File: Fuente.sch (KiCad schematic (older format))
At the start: 18 parts, among them J5 TB_1X2, P2 USB_OTG, U2 LM2596-5.0, U3 NCP1117ST33T3G

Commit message: Modifico algunos componentes. Seteo algunos encapsulados. Ordeno los componentes en el PCB.
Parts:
- removed TH1: PTS18126V300, ~, symbol THERMISTOR-RESCUE-ciaa-nxp
- removed U2: LM2596-5.0, ~, symbol LM2596-5.0
- removed ZA1: P6SMB33CA, ~, symbol TVS-RESCUE-ciaa-nxp
- added U2: LM2576HVS-5, TO_SOT_Packages_SMD:TO-263-5Lead, symbol LM2576HVS-5
- C6: footprint ~ -> Capacitors_ThroughHole:C_Radial_D13_L21_P5
- C7: value 330uF -> 1000uF; footprint ~ -> Capacitors_ThroughHole:C_Radial_D10_L20_P5
- C8: footprint ~ -> Capacitors_ThroughHole:C_Radial_D10_L25_P5
- D1, D3, FB1, FB2: footprint ~ -> Diodes_SMD:SOD-123
- D2: value B540C-13-F -> 1N5822; footprint ~ -> Diodes_SMD:SOD-123
- D4: footprint ~ -> LEDs:LED_1206
- J5: footprint ~ -> Connect:bornier2
- L1: value 47uH -> 100uH; footprint ~ -> Inductors:INDUCTOR_V
- P2: footprint (none) -> Connect:USB_Micro-B
- R1: footprint ~ -> SMD_Packages:SMD-1206_Pol
- U3: footprint ~ -> TO_SOT_Packages_SMD:SOT-323
- ZA2: footprint ~ -> Diodes_SMD:SMB_Handsoldering
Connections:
- net labels removed: +24V
- wire segments 47 -> 45
- no-connect marks 4 -> 5
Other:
- note removed: "Polyswitch"
- moved on the sheet: C6, D1, J5

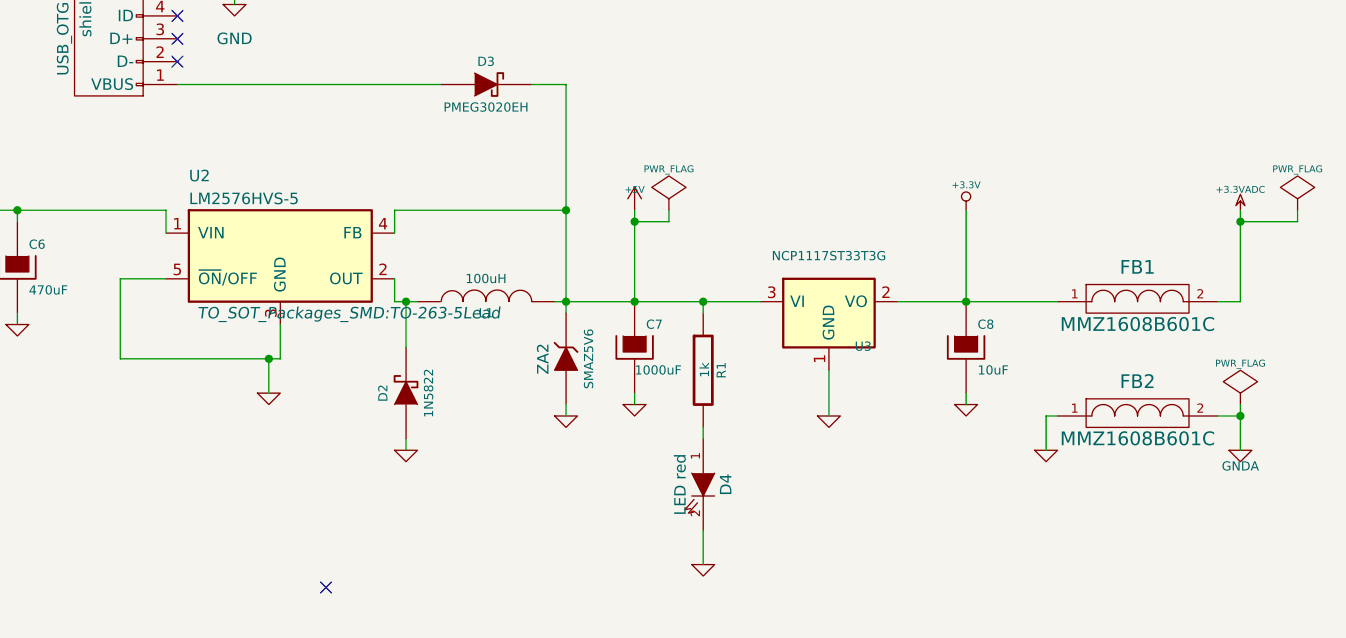
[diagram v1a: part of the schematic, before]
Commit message: Algunas modificaciones en el circuito  oreno el pcb.
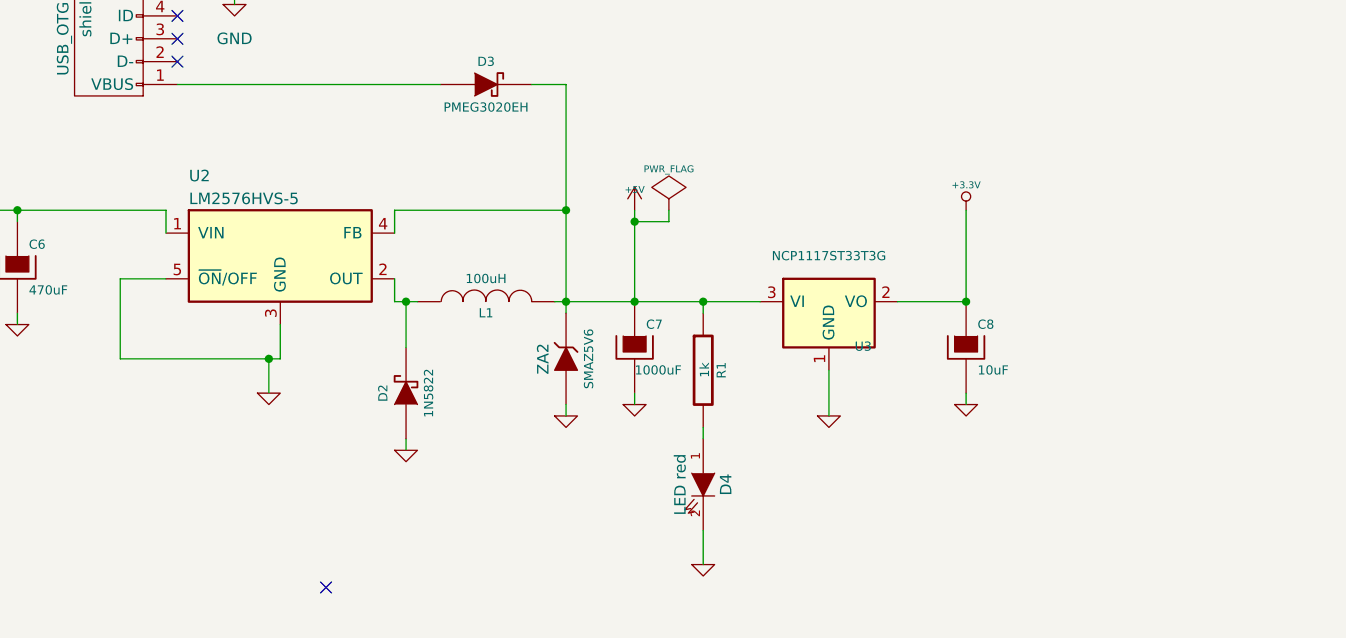
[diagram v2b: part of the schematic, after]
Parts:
- removed FB1, FB2: MMZ1608B601C, Diodes_SMD:SOD-123, symbol FILTER
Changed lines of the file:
@@
 LIBS:video
 LIBS:xilinx
+LIBS:sim800l
 EELAYER 25 0
 EELAYER END
@@
 encoding utf-8
 Sheet 3 6
-Title "CIAA Fuente de alimentación"
+Title "Fuente de alimentación"
 Date "11 may 2015"
 Rev "1.0"
@@
 Connection ~ 6900 3650
 Connection ~ 8050 3650
-Wire Wire Line
-	7750 3650 8450 3650
 $Comp
 L GND-RESCUE-ciaa-nxp #PWR014
@@
 	6300 4150 6300 4100
 $Comp
-L FILTER FB1
-U 1 1 581A28AB
-P 8800 3650
-F 0 "FB1" H 8800 3800 60  0000 C CNN
-F 1 "MMZ1608B601C" H 8800 3550 60  0000 C CNN
-F 2 "Diodes_SMD:SOD-123" H 8800 3650 60  0001 C CNN
-F 3 "~" H 8800 3650 60  0000 C CNN
-	1    8800 3650
-	1    0    0    -1
-$EndComp
-Wire Wire Line
-	9250 3650 9150 3650
-Wire Wire Line
-	9250 3250 9250 3650
-$Comp
 L +5V #PWR015
 U 1 1 581A28AD
@@
 $EndComp
 $Comp
-L +3.3VADC #PWR017
-U 1 1 581A28AF
-P 9250 3250
-F 0 "#PWR017" H 9250 3370 20  0001 C CNN
-F 1 "+3.3VADC" H 9250 3340 30  0000 C CNN
-F 2 "" H 9250 3250 60  0000 C CNN
-F 3 "" H 9250 3250 60  0000 C CNN
-	1    9250 3250
-	1    0    0    -1
-$EndComp
-$Comp
-L FILTER FB2
-U 1 1 581A28B0
-P 8800 4150
-F 0 "FB2" H 8800 4300 60  0000 C CNN
-F 1 "MMZ1608B601C" H 8800 4050 60  0000 C CNN
-F 2 "Diodes_SMD:SOD-123" H 8800 4150 60  0001 C CNN
-F 3 "~" H 8800 4150 60  0000 C CNN
-	1    8800 4150
-	1    0    0    -1
-$EndComp
-$Comp
-L GND-RESCUE-ciaa-nxp #PWR018
-U 1 1 581A28B1
-P 8400 4300
-F 0 "#PWR018" H 8400 4300 30  0001 C CNN
-F 1 "GND" H 8400 4230 30  0001 C CNN
-F 2 "" H 8400 4300 60  0000 C CNN
-F 3 "" H 8400 4300 60  0000 C CNN
-	1    8400 4300
-	1    0    0    -1
-$EndComp
-Wire Wire Line
-	8400 4150 8450 4150
-$Comp
-L GNDA-RESCUE-ciaa-nxp #PWR019
-U 1 1 581A28B2
-P 9250 4300
-F 0 "#PWR019" H 9250 4300 40  0001 C CNN
-F 1 "GNDA" H 9250 4230 40  0000 C CNN
-F 2 "" H 9250 4300 60  0000 C CNN
-F 3 "" H 9250 4300 60  0000 C CNN
-	1    9250 4300
-	1    0    0    -1
-$EndComp
-Wire Wire Line
-	9250 4100 9250 4300
-Wire Wire Line
-	9250 4150 9150 4150
-$Comp
-L PWR_FLAG #FLG020
+L PWR_FLAG #FLG017
 U 1 1 581A28B3
 P 6750 3250
-F 0 "#FLG020" H 6750 3345 30  0001 C CNN
+F 0 "#FLG017" H 6750 3345 30  0001 C CNN
 F 1 "PWR_FLAG" H 6750 3430 30  0000 C CNN
 F 2 "" H 6750 3250 60  0000 C CNN
@@
 	6750 3300 6600 3300
 Connection ~ 6600 3300
-$Comp
-L PWR_FLAG #FLG021
-U 1 1 581A28B4
-P 9500 3250
-F 0 "#FLG021" H 9500 3345 30  0001 C CNN
-F 1 "PWR_FLAG" H 9500 3430 30  0000 C CNN
-F 2 "" H 9500 3250 60  0000 C CNN
-F 3 "" H 9500 3250 60  0000 C CNN
-	1    9500 3250
-	1    0    0    -1
-$EndComp
-Wire Wire Line
-	9500 3250 9500 3300
-Wire Wire Line
-	9500 3300 9250 3300
-Connection ~ 9250 3300
-$Comp
-L PWR_FLAG #FLG022
-U 1 1 581A28B5
-P 9250 4100
-F 0 "#FLG022" H 9250 4195 30  0001 C CNN
-F 1 "PWR_FLAG" H 9250 4280 30  0000 C CNN
-F 2 "" H 9250 4100 60  0000 C CNN
-F 3 "" H 9250 4100 60  0000 C CNN
-	1    9250 4100
-	1    0    0    -1
-$EndComp
-Connection ~ 9250 4150
-Wire Wire Line
-	8400 4150 8400 4300
 Wire Wire Line
 	3500 3450 3500 3700
 $Comp
-L PWR_FLAG #FLG023
+L PWR_FLAG #FLG018
 U 1 1 581A28B7
 P 3350 3700
-F 0 "#FLG023" H 3350 3795 30  0001 C CNN
+F 0 "#FLG018" H 3350 3795 30  0001 C CNN
 F 1 "PWR_FLAG" H 3350 3880 30  0000 C CNN
 F 2 "" H 3350 3700 60  0000 C CNN
@@
 $EndComp
 $Comp
-L GND #PWR024
+L GND #PWR019
 U 1 1 581A28BC
 P 4850 2350
-F 0 "#PWR024" H 4850 2100 50  0001 C CNN
+F 0 "#PWR019" H 4850 2100 50  0001 C CNN
 F 1 "GND" H 4850 2200 50  0000 C CNN
 F 2 "" H 4850 2350 50  0000 C CNN
@@
 F 0 "U2" H 4650 3800 50  0000 L CNN
 F 1 "LM2576HVS-5" H 4650 3700 50  0000 L CNN
-F 2 "TO_SOT_Packages_SMD:TO-263-5Lead" H 5350 3200 50  0000 C CIN
+F 2 "TO_SOT_Packages_SMD:TO-263-5Lead" H 5350 3200 50  0001 C CIN
 F 3 "" H 5050 3450 50  0000 C CNN
 	1    5050 3450
@@
 Connection ~ 3900 3250
 NoConn ~ 5250 4900
+Wire Wire Line
+	7750 3650 8050 3650
 $EndSCHEMATC

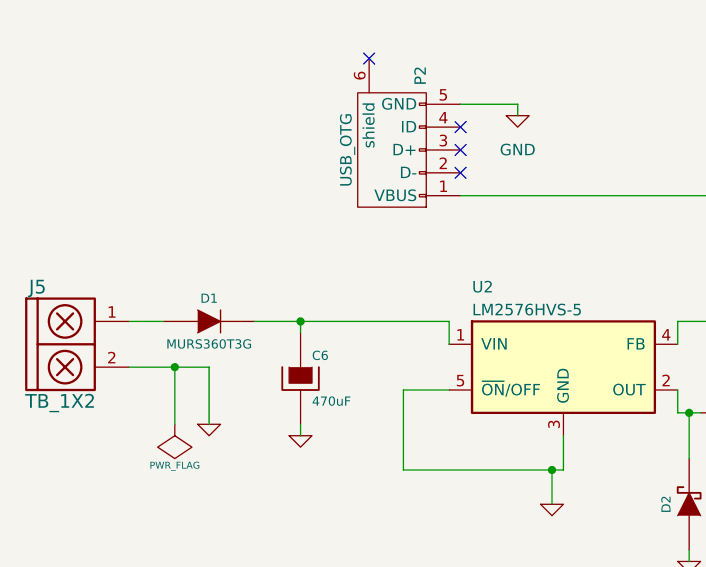
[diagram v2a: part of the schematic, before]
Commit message: Modificaciones en el schematic debida a los warning por powerflag y conectores mal definido como input en vez de pasive.
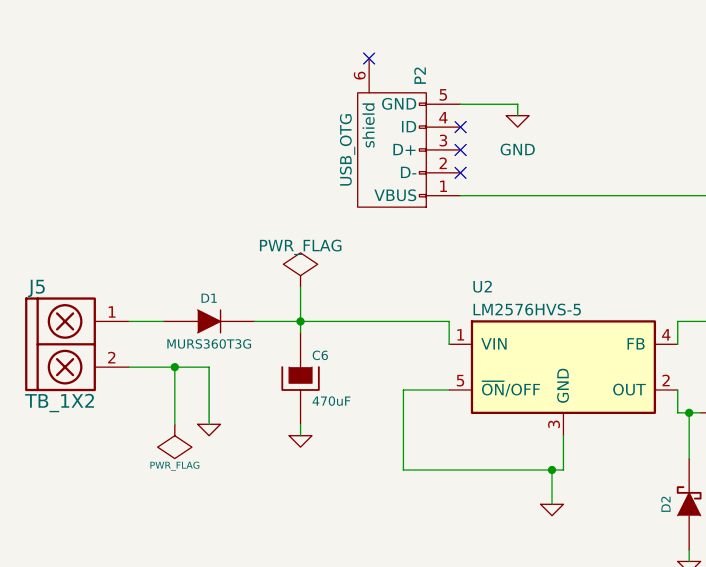
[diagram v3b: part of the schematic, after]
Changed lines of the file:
@@
 $Descr A4 11693 8268
 encoding utf-8
-Sheet 3 6
+Sheet 3 5
 Title "Fuente de alimentación"
 Date "11 may 2015"
@@
 $EndComp
 $Comp
-L GND-RESCUE-ciaa-nxp #PWR06
+L GND-RESCUE-ciaa-nxp #PWR011
 U 1 1 581A2897
 P 3500 3700
-F 0 "#PWR06" H 3500 3700 30  0001 C CNN
+F 0 "#PWR011" H 3500 3700 30  0001 C CNN
 F 1 "GND" H 3500 3630 30  0001 C CNN
 F 2 "" H 3500 3700 60  0000 C CNN
@@
 $EndComp
 $Comp
-L GND-RESCUE-ciaa-nxp #PWR07
+L GND-RESCUE-ciaa-nxp #PWR012
 U 1 1 581A2898
 P 3900 3750
-F 0 "#PWR07" H 3900 3750 30  0001 C CNN
+F 0 "#PWR012" H 3900 3750 30  0001 C CNN
 F 1 "GND" H 3900 3680 30  0001 C CNN
 F 2 "" H 3900 3750 60  0000 C CNN
@@
 $EndComp
 $Comp
-L GND-RESCUE-ciaa-nxp #PWR08
+L GND-RESCUE-ciaa-nxp #PWR013
 U 1 1 581A2899
 P 5000 4050
-F 0 "#PWR08" H 5000 4050 30  0001 C CNN
+F 0 "#PWR013" H 5000 4050 30  0001 C CNN
 F 1 "GND" H 5000 3980 30  0001 C CNN
 F 2 "" H 5000 4050 60  0000 C CNN
@@
 $EndComp
 $Comp
-L GND-RESCUE-ciaa-nxp #PWR09
+L GND-RESCUE-ciaa-nxp #PWR014
 U 1 1 581A289D
 P 5600 4300
-F 0 "#PWR09" H 5600 4300 30  0001 C CNN
+F 0 "#PWR014" H 5600 4300 30  0001 C CNN
 F 1 "GND" H 5600 4230 30  0001 C CNN
 F 2 "" H 5600 4300 60  0000 C CNN
@@
 $EndComp
 $Comp
-L GND-RESCUE-ciaa-nxp #PWR010
+L GND-RESCUE-ciaa-nxp #PWR015
 U 1 1 581A289F
 P 6600 4100
-F 0 "#PWR010" H 6600 4100 30  0001 C CNN
+F 0 "#PWR015" H 6600 4100 30  0001 C CNN
 F 1 "GND" H 6600 4030 30  0001 C CNN
 F 2 "" H 6600 4100 60  0000 C CNN
@@
 $EndComp
 $Comp
-L GND-RESCUE-ciaa-nxp #PWR011
+L GND-RESCUE-ciaa-nxp #PWR016
 U 1 1 581A28A0
 P 7450 4150
-F 0 "#PWR011" H 7450 4150 30  0001 C CNN
+F 0 "#PWR016" H 7450 4150 30  0001 C CNN
 F 1 "GND" H 7450 4080 30  0001 C CNN
 F 2 "" H 7450 4150 60  0000 C CNN
@@
 $EndComp
 $Comp
-L GND-RESCUE-ciaa-nxp #PWR012
+L GND-RESCUE-ciaa-nxp #PWR017
 U 1 1 581A28A2
 P 8050 4100
-F 0 "#PWR012" H 8050 4100 30  0001 C CNN
+F 0 "#PWR017" H 8050 4100 30  0001 C CNN
 F 1 "GND" H 8050 4030 30  0001 C CNN
 F 2 "" H 8050 4100 60  0000 C CNN
@@
 $EndComp
 $Comp
-L GND-RESCUE-ciaa-nxp #PWR013
+L GND-RESCUE-ciaa-nxp #PWR018
 U 1 1 581A28A9
 P 6900 4800
-F 0 "#PWR013" H 6900 4800 30  0001 C CNN
+F 0 "#PWR018" H 6900 4800 30  0001 C CNN
 F 1 "GND" H 6900 4730 30  0001 C CNN
 F 2 "" H 6900 4800 60  0000 C CNN
@@
 	1    0    0    -1
 $EndComp
-Wire Wire Line
-	6300 3250 5550 3250
-Wire Wire Line
-	6250 3650 7150 3650
-Wire Wire Line
-	6600 3250 6600 3650
-Connection ~ 6600 3650
-Wire Wire Line
-	7450 3950 7450 4150
-Wire Wire Line
-	8050 3650 8050 3250
-Wire Wire Line
-	4600 2700 5750 2700
-Wire Wire Line
-	6150 2700 6300 2700
-Connection ~ 6300 3250
-Connection ~ 6300 3650
-Wire Wire Line
-	3150 3250 3300 3250
-Wire Wire Line
-	3150 3450 3500 3450
-Wire Wire Line
-	6900 4200 6900 4250
-Wire Wire Line
-	6900 4650 6900 4800
-Wire Wire Line
-	6900 3700 6900 3650
-Connection ~ 6900 3650
-Connection ~ 8050 3650
-$Comp
-L GND-RESCUE-ciaa-nxp #PWR014
+$Comp
+L GND-RESCUE-ciaa-nxp #PWR019
 U 1 1 581A28AA
 P 6300 4150
-F 0 "#PWR014" H 6300 4150 30  0001 C CNN
+F 0 "#PWR019" H 6300 4150 30  0001 C CNN
 F 1 "GND" H 6300 4080 30  0001 C CNN
 F 2 "" H 6300 4150 60  0000 C CNN
@@
 	1    0    0    -1
 $EndComp
-Wire Wire Line
-	6300 4150 6300 4100
-$Comp
-L +5V #PWR015
+$Comp
+L +5V #PWR020
 U 1 1 581A28AD
 P 6600 3250
-F 0 "#PWR015" H 6600 3340 20  0001 C CNN
+F 0 "#PWR020" H 6600 3340 20  0001 C CNN
 F 1 "+5V" H 6600 3340 30  0000 C CNN
 F 2 "" H 6600 3250 60  0000 C CNN
@@
 $EndComp
 $Comp
-L +3.3V-RESCUE-ciaa-nxp #PWR016
+L +3.3V-RESCUE-ciaa-nxp #PWR021
 U 1 1 581A28AE
 P 8050 3250
-F 0 "#PWR016" H 8050 3210 30  0001 C CNN
+F 0 "#PWR021" H 8050 3210 30  0001 C CNN
 F 1 "+3.3V" H 8050 3360 30  0000 C CNN
 F 2 "" H 8050 3250 60  0000 C CNN
@@
 $EndComp
 $Comp
-L PWR_FLAG #FLG017
+L PWR_FLAG #FLG022
 U 1 1 581A28B3
 P 6750 3250
-F 0 "#FLG017" H 6750 3345 30  0001 C CNN
+F 0 "#FLG022" H 6750 3345 30  0001 C CNN
 F 1 "PWR_FLAG" H 6750 3430 30  0000 C CNN
 F 2 "" H 6750 3250 60  0000 C CNN
@@
 	1    0    0    -1
 $EndComp
-Wire Wire Line
-	6750 3250 6750 3300
-Wire Wire Line
-	6750 3300 6600 3300
-Connection ~ 6600 3300
-Wire Wire Line
-	3500 3450 3500 3700
-$Comp
-L PWR_FLAG #FLG018
+$Comp
+L PWR_FLAG #FLG023
 U 1 1 581A28B7
 P 3350 3700
-F 0 "#FLG018" H 3350 3795 30  0001 C CNN
+F 0 "#FLG023" H 3350 3795 30  0001 C CNN
 F 1 "PWR_FLAG" H 3350 3880 30  0000 C CNN
 F 2 "" H 3350 3700 60  0000 C CNN
@@
 	-1   0    0    1
 $EndComp
-Wire Wire Line
-	3350 3700 3350 3450
-Connection ~ 3350 3450
 Text Notes 5700 5400 0    60   ~ 0
 Reemplazo SMD del 1N5825.
@@
 	0    -1   -1   0
 $EndComp
-Wire Wire Line
-	6300 2700 6300 3700
-Wire Wire Line
-	3900 3750 3900 3700
-Wire Wire Line
-	6600 4100 6600 4050
-Wire Wire Line
-	8050 4100 8050 4050
-Wire Wire Line
-	5600 4250 5600 4300
-Wire Wire Line
-	5550 3650 5650 3650
-Wire Wire Line
-	5600 3850 5600 3650
-Connection ~ 5600 3650
 $Comp
 L USB_OTG-RESCUE-ciaa-nxp P2
@@
 $EndComp
 $Comp
-L GND #PWR019
+L GND #PWR024
 U 1 1 581A28BC
 P 4850 2350
-F 0 "#PWR019" H 4850 2100 50  0001 C CNN
+F 0 "#PWR024" H 4850 2100 50  0001 C CNN
 F 1 "GND" H 4850 2200 50  0000 C CNN
 F 2 "" H 4850 2350 50  0000 C CNN
@@
 	1    0    0    -1
 $EndComp
-Wire Wire Line
-	4600 2300 4850 2300
-Wire Wire Line
-	4850 2300 4850 2350
 NoConn ~ 4600 2400
 NoConn ~ 4600 2500
 NoConn ~ 4600 2600
 NoConn ~ 4200 2100
+NoConn ~ 5250 4900
 $Comp
 L LM2576HVS-5 U2
@@
 $EndComp
 Wire Wire Line
+	4550 3250 4550 3350
+Wire Wire Line
+	3700 3250 4550 3250
+Wire Wire Line
+	7750 3650 8050 3650
+Connection ~ 3900 3250
+Wire Wire Line
+	3900 3100 3900 3300
+Wire Wire Line
+	5550 3250 5550 3350
+Wire Wire Line
+	5550 3650 5550 3550
+Connection ~ 5000 3900
+Wire Wire Line
+	5000 3900 5000 4050
+Wire Wire Line
+	5050 3900 5050 3750
+Wire Wire Line
+	4350 3900 5050 3900
+Wire Wire Line
+	4350 3550 4350 3900
+Wire Wire Line
 	4550 3550 4350 3550
 Wire Wire Line
-	4350 3550 4350 3900
-Wire Wire Line
-	4350 3900 5050 3900
-Wire Wire Line
-	5050 3900 5050 3750
-Wire Wire Line
-	5000 3900 5000 4050
-Connection ~ 5000 3900
-Wire Wire Line
-	5550 3650 5550 3550
-Wire Wire Line
-	5550 3250 5550 3350
-Wire Wire Line
-	4550 3250 4550 3350
-Wire Wire Line
-	3700 3250 4550 3250
-Wire Wire Line
-	3900 3300 3900 3250
-Connection ~ 3900 3250
-NoConn ~ 5250 4900
-Wire Wire Line
-	7750 3650 8050 3650
+	4850 2300 4850 2350
+Wire Wire Line
+	4600 2300 4850 2300
+Connection ~ 5600 3650
+Wire Wire Line
+	5600 3850 5600 3650
+Wire Wire Line
+	5550 3650 5650 3650
+Wire Wire Line
+	5600 4250 5600 4300
+Wire Wire Line
+	8050 4100 8050 4050
+Wire Wire Line
+	6600 4100 6600 4050
+Wire Wire Line
+	3900 3750 3900 3700
+Wire Wire Line
+	6300 2700 6300 3700
+Connection ~ 3350 3450
+Wire Wire Line
+	3350 3700 3350 3450
+Wire Wire Line
+	3500 3450 3500 3700
+Connection ~ 6600 3300
+Wire Wire Line
+	6750 3300 6600 3300
+Wire Wire Line
+	6750 3250 6750 3300
+Wire Wire Line
+	6300 4150 6300 4100
+Connection ~ 8050 3650
+Connection ~ 6900 3650
+Wire Wire Line
+	6900 3700 6900 3650
+Wire Wire Line
+	6900 4650 6900 4800
+Wire Wire Line
+	6900 4200 6900 4250
+Wire Wire Line
+	3150 3450 3500 3450
+Wire Wire Line
+	3150 3250 3300 3250
+Connection ~ 6300 3650
+Connection ~ 6300 3250
+Wire Wire Line
+	6150 2700 6300 2700
+Wire Wire Line
+	4600 2700 5750 2700
+Wire Wire Line
+	8050 3650 8050 3250
+Wire Wire Line
+	7450 3950 7450 4150
+Connection ~ 6600 3650
+Wire Wire Line
+	6600 3250 6600 3650
+Wire Wire Line
+	6250 3650 7150 3650
+Wire Wire Line
+	6300 3250 5550 3250
+$Comp
+L PWR_FLAG #FLG025
+U 1 1 581E77AD
+P 3900 3100
+F 0 "#FLG025" H 3900 3195 50  0001 C CNN
+F 1 "PWR_FLAG" H 3900 3280 50  0000 C CNN
+F 2 "" H 3900 3100 50  0000 C CNN
+F 3 "" H 3900 3100 50  0000 C CNN
+	1    3900 3100
+	1    0    0    -1
+$EndComp
 $EndSCHEMATC
